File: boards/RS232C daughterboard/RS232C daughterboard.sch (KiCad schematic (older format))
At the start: 1 part, among them P0 HEADER

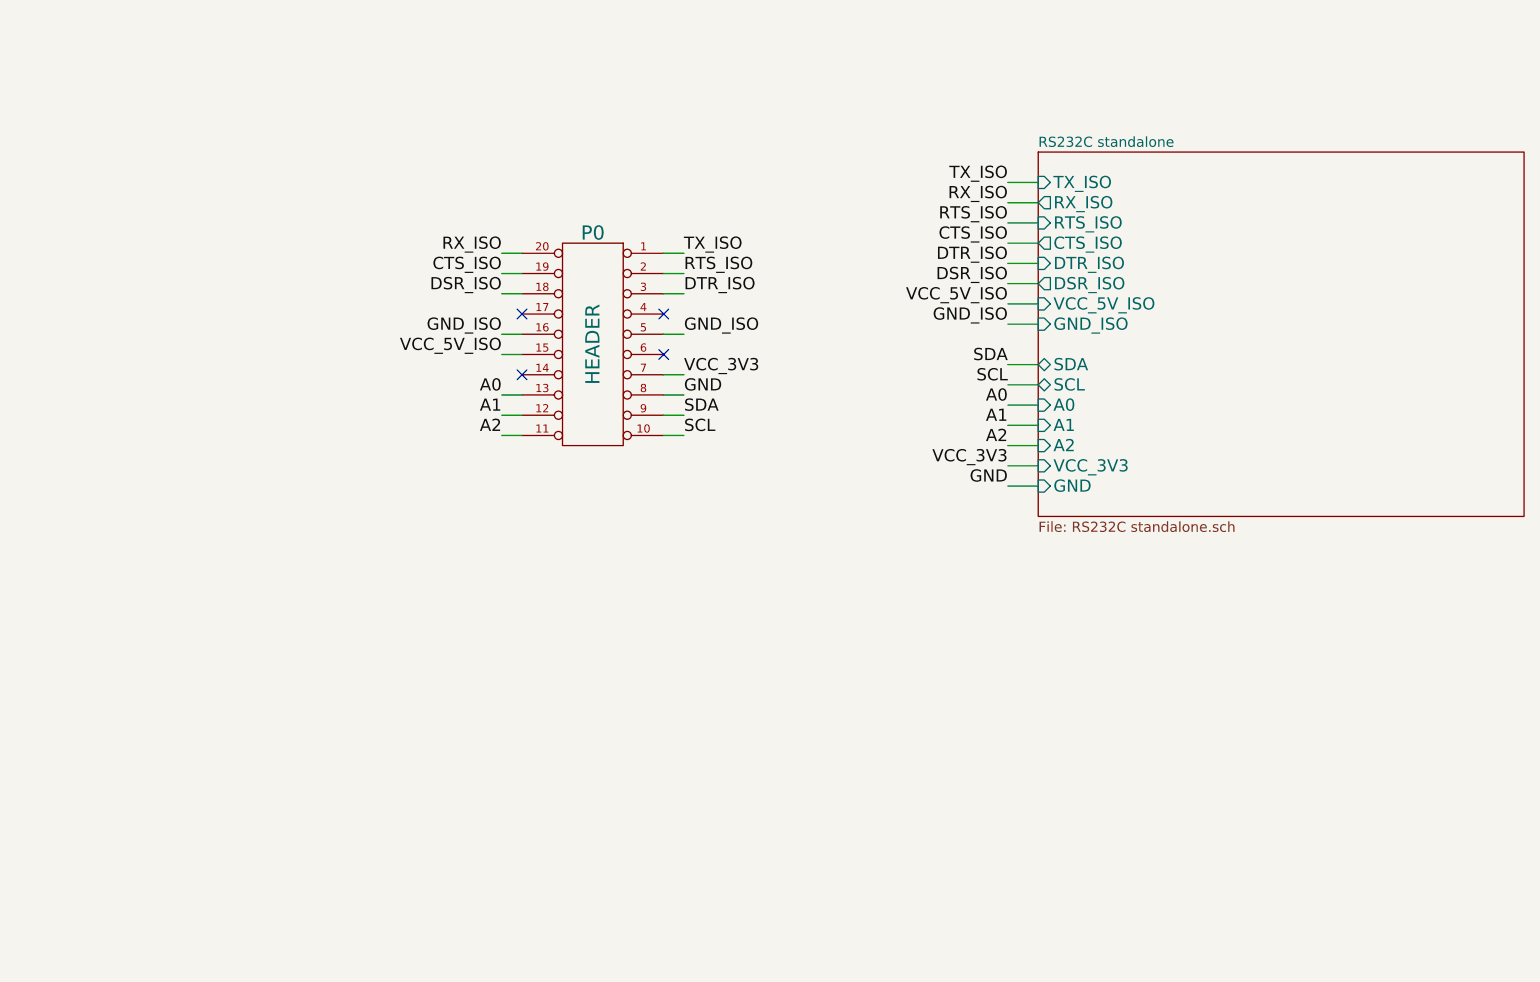
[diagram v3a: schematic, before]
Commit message: Improved main sheet of RS232C daughterboard
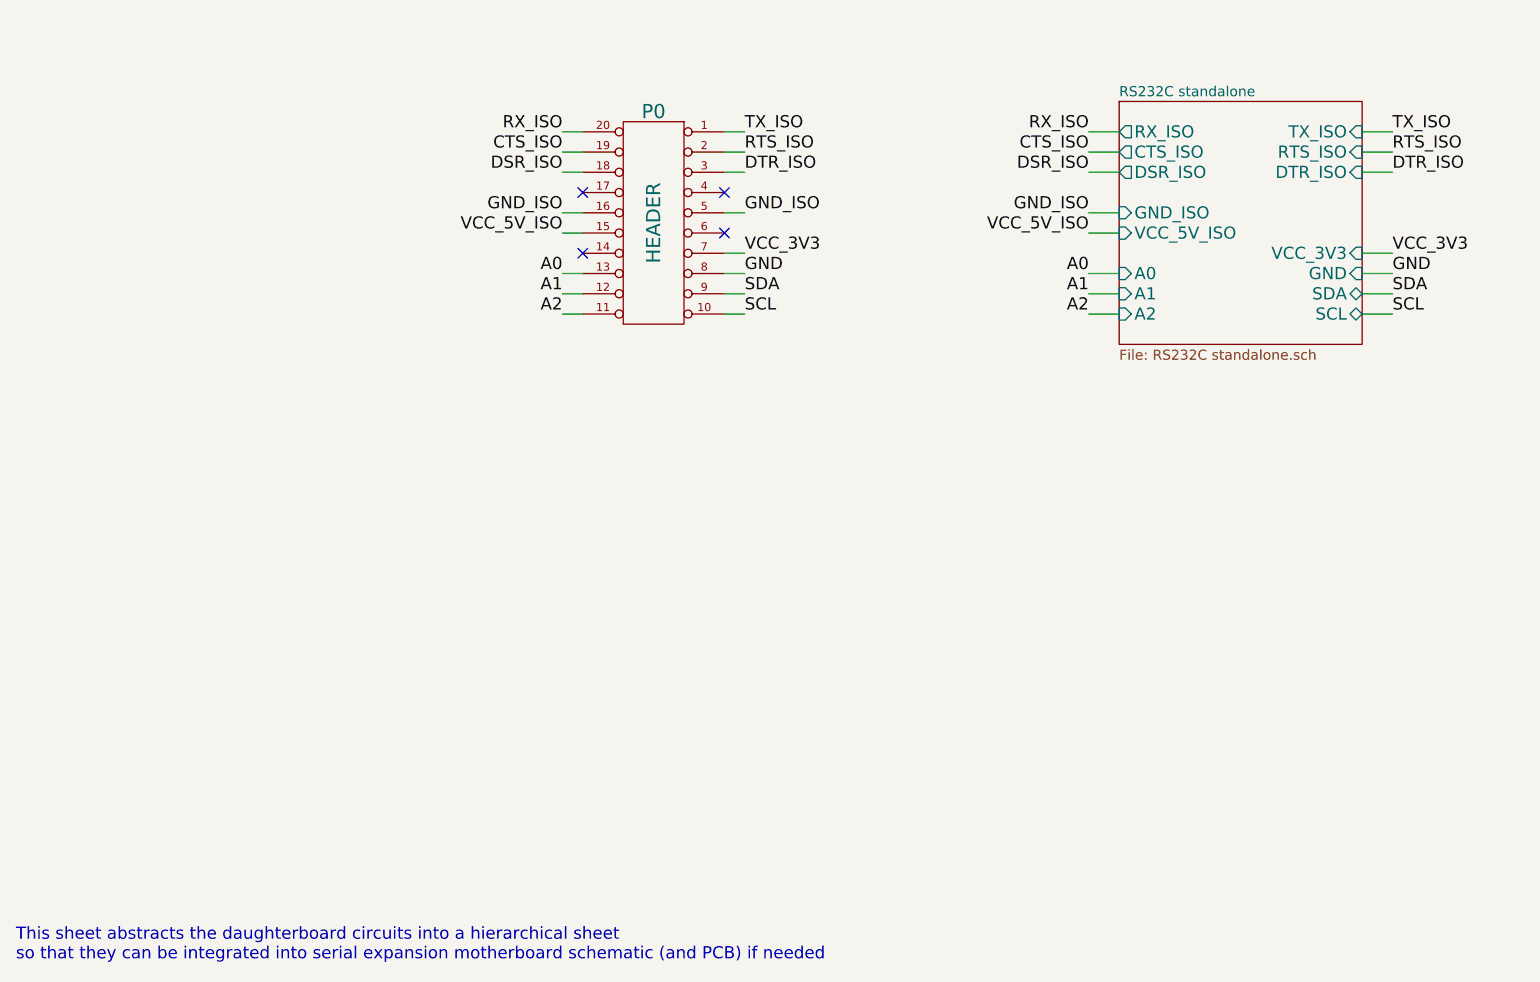
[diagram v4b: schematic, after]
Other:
- note added: "This sheet abstracts the daughterboard circuits into a hierarchical sheet \nso that they can be integrated into serial expansion motherboard schematic (and PCB) if needed"
- moved on the sheet: P0
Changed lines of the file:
@@
 L DIL20 P0
 U 1 1 53AB69C0
-P 3800 4300
-F 0 "P0" H 3800 4850 70  0000 C CNN
-F 1 "HEADER" V 3800 4300 70  0000 C CNN
-F 2 "" H 3800 4300 60  0000 C CNN
-F 3 "" H 3800 4300 60  0000 C CNN
-	1    3800 4300
+P 4100 3700
+F 0 "P0" H 4100 4250 70  0000 C CNN
+F 1 "HEADER" V 4100 3700 70  0000 C CNN
+F 2 "" H 4100 3700 60  0000 C CNN
+F 3 "" H 4100 3700 60  0000 C CNN
+	1    4100 3700
 	-1   0    0    -1
 $EndComp
 $Sheet
-S 6000 3350 2400 1800
+S 6400 3100 1200 1200
 U 53AB69CE
 F0 "RS232C standalone" 50
 F1 "RS232C standalone.sch" 50
-F2 "TX_ISO" I L 6000 3500 60
-F3 "RX_ISO" O L 6000 3600 60
-F4 "RTS_ISO" I L 6000 3700 60
-F5 "CTS_ISO" O L 6000 3800 60
-F6 "DTR_ISO" I L 6000 3900 60
-F7 "DSR_ISO" O L 6000 4000 60
-F8 "VCC_3V3" I L 6000 4900 60
-F9 "GND" I L 6000 5000 60
-F10 "VCC_5V_ISO" I L 6000 4100 60
-F11 "GND_ISO" I L 6000 4200 60
-F12 "SDA" B L 6000 4400 60
-F13 "SCL" B L 6000 4500 60
-F14 "A0" I L 6000 4600 60
-F15 "A1" I L 6000 4700 60
-F16 "A2" I L 6000 4800 60
+F2 "TX_ISO" I R 7600 3250 60
+F3 "RX_ISO" O L 6400 3250 60
+F4 "RTS_ISO" I R 7600 3350 60
+F5 "CTS_ISO" O L 6400 3350 60
+F6 "DTR_ISO" I R 7600 3450 60
+F7 "DSR_ISO" O L 6400 3450 60
+F8 "VCC_3V3" I R 7600 3850 60
+F9 "GND" I R 7600 3950 60
+F10 "VCC_5V_ISO" I L 6400 3750 60
+F11 "GND_ISO" I L 6400 3650 60
+F12 "SDA" B R 7600 4050 60
+F13 "SCL" B R 7600 4150 60
+F14 "A0" I L 6400 3950 60
+F15 "A1" I L 6400 4050 60
+F16 "A2" I L 6400 4150 60
 $EndSheet
 Wire Wire Line
-	3450 3850 3350 3850
+	3750 3250 3650 3250
 Wire Wire Line
-	3450 3950 3350 3950
+	3750 3350 3650 3350
 Wire Wire Line
-	3450 4050 3350 4050
+	3750 3450 3650 3450
 Wire Wire Line
-	3450 4250 3350 4250
+	3750 3650 3650 3650
 Wire Wire Line
-	3450 4350 3350 4350
+	3750 3750 3650 3750
 Wire Wire Line
-	3450 4550 3350 4550
+	3750 3950 3650 3950
 Wire Wire Line
-	4250 3850 4150 3850
+	4550 3250 4450 3250
 Wire Wire Line
-	4250 3950 4150 3950
+	4550 3350 4450 3350
 Wire Wire Line
-	4250 4050 4150 4050
+	4550 3450 4450 3450
 Wire Wire Line
-	4250 4250 4150 4250
+	4550 3650 4450 3650
 Wire Wire Line
-	4250 4450 4150 4450
+	4550 3850 4450 3850
 Wire Wire Line
-	4250 4550 4150 4550
+	4550 3950 4450 3950
 Wire Wire Line
-	3450 4650 3350 4650
+	3750 4050 3650 4050
 Wire Wire Line
-	3450 4750 3350 4750
+	3750 4150 3650 4150
 Wire Wire Line
-	4250 4650 4150 4650
+	4550 4050 4450 4050
 Wire Wire Line
-	4250 4750 4150 4750
-Text Label 4250 3850 0    60   ~ 0
+	4550 4150 4450 4150
+Text Label 4550 3250 0    60   ~ 0
 TX_ISO
-Text Label 4250 3950 0    60   ~ 0
+Text Label 4550 3350 0    60   ~ 0
 RTS_ISO
-Text Label 4250 4050 0    60   ~ 0
+Text Label 4550 3450 0    60   ~ 0
 DTR_ISO
-Text Label 4250 4450 0    60   ~ 0
+Text Label 4550 3850 0    60   ~ 0
 VCC_3V3
-Text Label 4250 4550 0    60   ~ 0
+Text Label 4550 3950 0    60   ~ 0
 GND
-Text Label 4250 4650 0    60   ~ 0
+Text Label 4550 4050 0    60   ~ 0
 SDA
-Text Label 4250 4750 0    60   ~ 0
+Text Label 4550 4150 0    60   ~ 0
 SCL
-Text Label 3350 4750 2    60   ~ 0
+Text Label 3650 4150 2    60   ~ 0
 A2
-Text Label 3350 4650 2    60   ~ 0
+Text Label 3650 4050 2    60   ~ 0
 A1
-Text Label 3350 4550 2    60   ~ 0
+Text Label 3650 3950 2    60   ~ 0
 A0
-Text Label 3350 4350 2    60   ~ 0
+Text Label 3650 3750 2    60   ~ 0
 VCC_5V_ISO
-Text Label 3350 4250 2    60   ~ 0
+Text Label 3650 3650 2    60   ~ 0
 GND_ISO
-Text Label 3350 4050 2    60   ~ 0
+Text Label 3650 3450 2    60   ~ 0
 DSR_ISO
-Text Label 3350 3950 2    60   ~ 0
+Text Label 3650 3350 2    60   ~ 0
 CTS_ISO
-Text Label 3350 3850 2    60   ~ 0
+Text Label 3650 3250 2    60   ~ 0
 RX_ISO
-Text Label 4250 4250 0    60   ~ 0
+Text Label 4550 3650 0    60   ~ 0
 GND_ISO
-NoConn ~ 4150 4350
-NoConn ~ 4150 4150
-NoConn ~ 3450 4150
-NoConn ~ 3450 4450
+NoConn ~ 4450 3750
+NoConn ~ 4450 3550
+NoConn ~ 3750 3550
+NoConn ~ 3750 3850
 Wire Wire Line
-	6000 3600 5850 3600
-Text Label 5850 3600 2    60   ~ 0
+	6400 3250 6250 3250
+Text Label 6250 3250 2    60   ~ 0
 RX_ISO
 Wire Wire Line
-	6000 3800 5850 3800
-Text Label 5850 3800 2    60   ~ 0
+	6400 3350 6250 3350
+Text Label 6250 3350 2    60   ~ 0
 CTS_ISO
 Wire Wire Line
-	6000 4000 5850 4000
-Text Label 5850 4000 2    60   ~ 0
+	6400 3450 6250 3450
+Text Label 6250 3450 2    60   ~ 0
 DSR_ISO
 Wire Wire Line
-	5850 3500 6000 3500
-Text Label 5850 3500 2    60   ~ 0
+	7750 3250 7600 3250
+Text Label 7750 3250 0    60   ~ 0
 TX_ISO
 Wire Wire Line
-	5850 3700 6000 3700
+	7750 3350 7600 3350
 Wire Wire Line
-	5850 3900 6000 3900
-Text Label 5850 3700 2    60   ~ 0
+	7750 3450 7600 3450
+Text Label 7750 3350 0    60   ~ 0
 RTS_ISO
-Text Label 5850 3900 2    60   ~ 0
+Text Label 7750 3450 0    60   ~ 0
 DTR_ISO
 Wire Wire Line
-	6000 4100 5850 4100
-Text Label 5850 4100 2    60   ~ 0
+	6400 3750 6250 3750
+Text Label 6250 3750 2    60   ~ 0
 VCC_5V_ISO
 Wire Wire Line
-	6000 4200 5850 4200
-Text Label 5850 4200 2    60   ~ 0
+	6400 3650 6250 3650
+Text Label 6250 3650 2    60   ~ 0
 GND_ISO
 Wire Wire Line
-	6000 4600 5850 4600
+	6400 3950 6250 3950
 Wire Wire Line
-	6000 4700 5850 4700
+	6400 4050 6250 4050
 Wire Wire Line
-	6000 4800 5850 4800
-Text Label 5850 4800 2    60   ~ 0
+	6400 4150 6250 4150
+Text Label 6250 4150 2    60   ~ 0
 A2
-Text Label 5850 4700 2    60   ~ 0
+Text Label 6250 4050 2    60   ~ 0
 A1
-Text Label 5850 4600 2    60   ~ 0
+Text Label 6250 3950 2    60   ~ 0
 A0
 Wire Wire Line
-	5850 4400 6000 4400
+	7750 4050 7600 4050
 Wire Wire Line
-	5850 4500 6000 4500
-Text Label 5850 4400 2    60   ~ 0
+	7750 4150 7600 4150
+Text Label 7750 4050 0    60   ~ 0
 SDA
-Text Label 5850 4500 2    60   ~ 0
+Text Label 7750 4150 0    60   ~ 0
 SCL
 Wire Wire Line
-	5850 5000 6000 5000
-Text Label 5850 4900 2    60   ~ 0
+	7750 3950 7600 3950
+Text Label 7750 3850 0    60   ~ 0
 VCC_3V3
-Text Label 5850 5000 2    60   ~ 0
+Text Label 7750 3950 0    60   ~ 0
 GND
 Wire Wire Line
-	6000 4900 5850 4900
+	7600 3850 7750 3850
+Text Notes 950  7350 0    60   ~ 0
+This sheet abstracts the daughterboard circuits into a hierarchical sheet \nso that they can be integrated into serial expansion motherboard schematic (and PCB) if needed
 $EndSCHEMATC

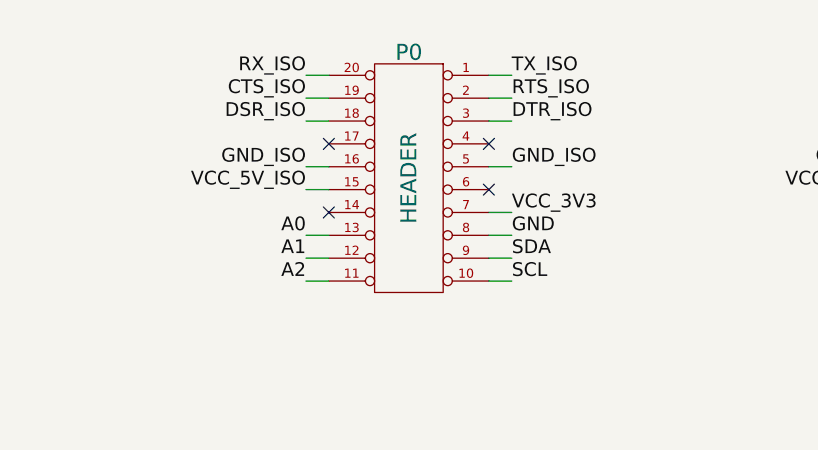
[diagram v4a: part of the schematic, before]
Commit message: Updated daughterboard header pinout in all sheets to be PMOD UART 4/4A compatible
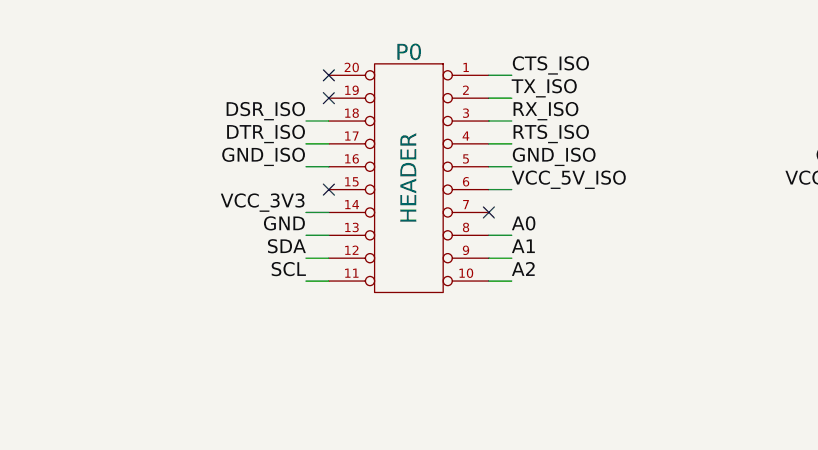
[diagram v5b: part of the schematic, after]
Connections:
- net A0: now also P0.8 (P8); no longer P0.13 (P13)
- net A1: now also P0.9 (P9); no longer P0.12 (P12)
- net A2: now also P0.10 (P10); no longer P0.11 (P11)
- net CTS_ISO: now also P0.1 (P1); no longer P0.19 (P19)
- net DTR_ISO: now also P0.17 (P17); no longer P0.3 (P3)
- net GND: now also P0.13 (P13); no longer P0.8 (P8)
- net RTS_ISO: now also P0.4 (P4); no longer P0.2 (P2)
- net RX_ISO: now also P0.3 (P3); no longer P0.20 (P20)
- net SCL: now also P0.11 (P11); no longer P0.10 (P10)
- net SDA: now also P0.12 (P12); no longer P0.9 (P9)
- net TX_ISO: now also P0.2 (P2); no longer P0.1 (P1)
- net VCC_3V3: now also P0.14 (P14); no longer P0.7 (P7)
- net VCC_5V_ISO: now also P0.6 (P6); no longer P0.15 (P15)
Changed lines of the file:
@@
 Sheet 1 2
 Title ""
-Date "26 jun 2014"
+Date "1 jul 2014"
 Rev ""
 Comp ""
@@
 $EndSheet
 Wire Wire Line
-	3750 3250 3650 3250
-Wire Wire Line
-	3750 3350 3650 3350
-Wire Wire Line
 	3750 3450 3650 3450
 Wire Wire Line
-	3750 3650 3650 3650
+	3750 3550 3650 3550
 Wire Wire Line
-	3750 3750 3650 3750
+	4450 3650 4550 3650
 Wire Wire Line
-	3750 3950 3650 3950
+	4450 3750 4550 3750
+Wire Wire Line
+	4450 3950 4550 3950
 Wire Wire Line
 	4550 3250 4450 3250
@@
 	4550 3450 4450 3450
 Wire Wire Line
-	4550 3650 4450 3650
+	3650 3650 3750 3650
 Wire Wire Line
-	4550 3850 4450 3850
+	3650 3850 3750 3850
 Wire Wire Line
-	4550 3950 4450 3950
+	3650 3950 3750 3950
 Wire Wire Line
-	3750 4050 3650 4050
+	4450 4050 4550 4050
 Wire Wire Line
-	3750 4150 3650 4150
+	4450 4150 4550 4150
 Wire Wire Line
-	4550 4050 4450 4050
+	3650 4050 3750 4050
 Wire Wire Line
-	4550 4150 4450 4150
+	3650 4150 3750 4150
 Text Label 4550 3250 0    60   ~ 0
+CTS_ISO
+Text Label 4550 3350 0    60   ~ 0
 TX_ISO
-Text Label 4550 3350 0    60   ~ 0
-RTS_ISO
 Text Label 4550 3450 0    60   ~ 0
+RX_ISO
+Text Label 3650 3850 2    60   ~ 0
+VCC_3V3
+Text Label 3650 3950 2    60   ~ 0
+GND
+Text Label 3650 4050 2    60   ~ 0
+SDA
+Text Label 3650 4150 2    60   ~ 0
+SCL
+Text Label 4550 4150 0    60   ~ 0
+A2
+Text Label 4550 4050 0    60   ~ 0
+A1
+Text Label 4550 3950 0    60   ~ 0
+A0
+Text Label 4550 3750 0    60   ~ 0
+VCC_5V_ISO
+Text Label 4550 3650 0    60   ~ 0
+GND_ISO
+Text Label 3650 3550 2    60   ~ 0
 DTR_ISO
-Text Label 4550 3850 0    60   ~ 0
-VCC_3V3
-Text Label 4550 3950 0    60   ~ 0
-GND
-Text Label 4550 4050 0    60   ~ 0
-SDA
-Text Label 4550 4150 0    60   ~ 0
-SCL
-Text Label 3650 4150 2    60   ~ 0
-A2
-Text Label 3650 4050 2    60   ~ 0
-A1
-Text Label 3650 3950 2    60   ~ 0
-A0
-Text Label 3650 3750 2    60   ~ 0
-VCC_5V_ISO
+Text Label 3650 3450 2    60   ~ 0
+DSR_ISO
 Text Label 3650 3650 2    60   ~ 0
 GND_ISO
-Text Label 3650 3450 2    60   ~ 0
-DSR_ISO
-Text Label 3650 3350 2    60   ~ 0
-CTS_ISO
-Text Label 3650 3250 2    60   ~ 0
-RX_ISO
-Text Label 4550 3650 0    60   ~ 0
-GND_ISO
-NoConn ~ 4450 3750
-NoConn ~ 4450 3550
-NoConn ~ 3750 3550
-NoConn ~ 3750 3850
+NoConn ~ 4450 3850
+NoConn ~ 3750 3750
 Wire Wire Line
 	6400 3250 6250 3250
@@
 Text Notes 950  7350 0    60   ~ 0
 This sheet abstracts the daughterboard circuits into a hierarchical sheet \nso that they can be integrated into serial expansion motherboard schematic (and PCB) if needed
+Wire Wire Line
+	4450 3550 4550 3550
+Text Label 4550 3550 0    60   ~ 0
+RTS_ISO
+NoConn ~ 3750 3350
+NoConn ~ 3750 3250
 $EndSCHEMATC

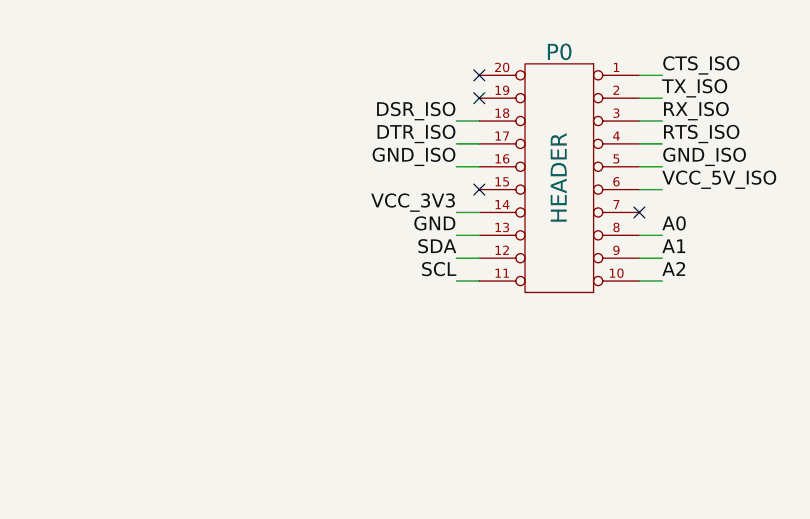
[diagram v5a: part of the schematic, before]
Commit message: Rearranged EEPROM pins in dboard slot pinout to be compatible with PMOD I2C interface
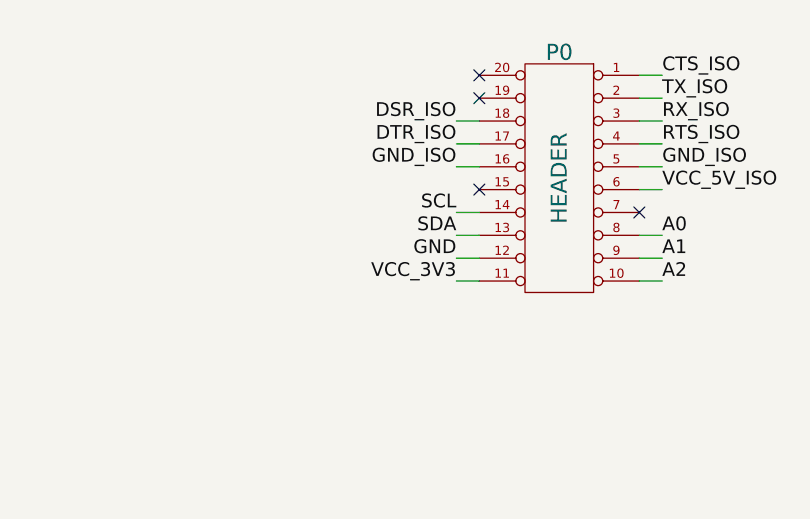
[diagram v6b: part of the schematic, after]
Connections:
- net GND: now also P0.12 (P12); no longer P0.13 (P13)
- net SCL: now also P0.14 (P14); no longer P0.11 (P11)
- net SDA: now also P0.13 (P13); no longer P0.12 (P12)
- net VCC_3V3: now also P0.11 (P11); no longer P0.14 (P14)
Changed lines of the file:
@@
 Sheet 1 2
 Title ""
-Date "1 jul 2014"
+Date "2 jul 2014"
 Rev ""
 Comp ""
@@
 	3650 3650 3750 3650
 Wire Wire Line
-	3650 3850 3750 3850
+	3650 4150 3750 4150
 Wire Wire Line
-	3650 3950 3750 3950
+	3650 4050 3750 4050
 Wire Wire Line
 	4450 4050 4550 4050
@@
 	4450 4150 4550 4150
 Wire Wire Line
-	3650 4050 3750 4050
+	3650 3950 3750 3950
 Wire Wire Line
-	3650 4150 3750 4150
+	3650 3850 3750 3850
 Text Label 4550 3250 0    60   ~ 0
 CTS_ISO
@@
 Text Label 4550 3450 0    60   ~ 0
 RX_ISO
+Text Label 3650 4150 2    60   ~ 0
+VCC_3V3
+Text Label 3650 4050 2    60   ~ 0
+GND
+Text Label 3650 3950 2    60   ~ 0
+SDA
 Text Label 3650 3850 2    60   ~ 0
-VCC_3V3
-Text Label 3650 3950 2    60   ~ 0
-GND
-Text Label 3650 4050 2    60   ~ 0
-SDA
-Text Label 3650 4150 2    60   ~ 0
 SCL
 Text Label 4550 4150 0    60   ~ 0
